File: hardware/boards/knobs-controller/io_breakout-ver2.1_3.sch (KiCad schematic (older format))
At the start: 34 parts, among them J27 Conn_01x01_Female, J28 Conn_01x01_Female, J29 Conn_01x01_Female, J30 Conn_01x01_Female, J31 Conn_01x01_Female, J32 Conn_01x01_Female, J33 Conn_01x01_Female, J34 Conn_01x01_Female, J35 Conn_01x01_Female, J36 Conn_01x01_Female, J37 Conn_01x01_Female, J38 Conn_01x01_Female, J39 Conn_01x01_Female, J40 Conn_01x01_Female, J41 Conn_01x01_Female, J42 Conn_01x01_Female, J43 Conn_01x01_Female, J44 Conn_01x01_Female, J45 Conn_01x01_Female, J46 Conn_01x01_Female, J47 Conn_01x01_Female, J48 Conn_01x01_Female, J49 Conn_01x01_Female, J50 Conn_01x01_Female, J51 Conn_01x01_Female, J52 Conn_01x01_Female, J53 Conn_01x01_Female, J54 Conn_01x01_Female, J55 Conn_01x01_Female, J56 Conn_01x01_Female, J57 WURTH_ELECTRONICS_61400413321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, J58 USB-A-S-X-X-VT

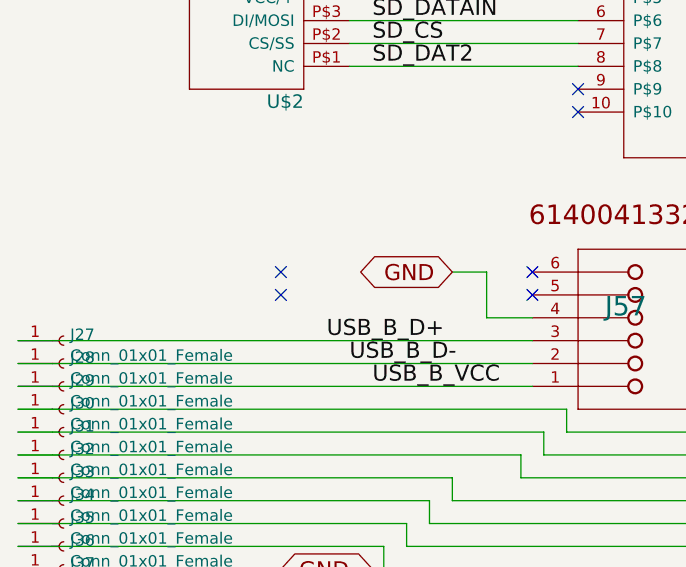
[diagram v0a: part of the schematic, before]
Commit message: changed c6 to 0805, updates to footprints to simplify BOM
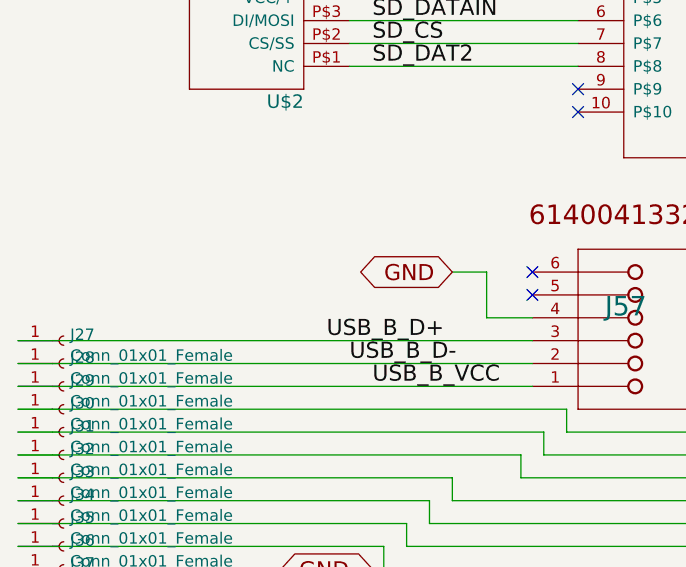
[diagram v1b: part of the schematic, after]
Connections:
- no-connect marks 10 -> 8
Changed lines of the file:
@@
 NoConn ~ 2500 2800
 NoConn ~ 2500 2900
-NoConn ~ 1400 2900
-NoConn ~ 1400 2800
 NoConn ~ 4750 3100
 NoConn ~ 4750 3000
